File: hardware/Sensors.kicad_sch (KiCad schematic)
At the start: 21 parts, among them J10 Right Photo Cell, J11 Front Center Distance Sensor, J12 Back Center Distance Sensor, J13 Bumper Switch 1, J14 Bumper Switch 2, J15 Bumper Switch 3, J16 PIR Sensor, J17 Front Right Distance Sensor, J18 Back Right Distance Sensor, J19 Left Cliff Sensor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

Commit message: First revision of the shield PCB
I have a few more tweaks that I would like to make before I send this
off to be manufactured. I ended up going with a 4 layer board as it has
signal wires going all over the place since I was a bit contrained with
part placement by most of the Arduino signal pins being on the right
side of the board and wanting to place connectors on the side closest
to the part to which they connect.
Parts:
- removed J12: Back Center Distance Sensor, Connector_PinSocket_2.54mm:PinSocket_1x07_P2.54mm_Vertical, symbol Connector_Generic:Conn_01x07
- J13, J14, J15: footprint Connector_PinSocket_2.54mm:PinSocket_1x02_P2.54mm_Vertical -> Connector_PinSocket_2.54mm:PinSocket_1x02_P2.54mm_Horizontal
- J19, J20: footprint Connector_PinSocket_2.54mm:PinSocket_1x07_P2.54mm_Vertical -> Connector_PinSocket_2.54mm:PinSocket_1x07_P2.54mm_Horizontal
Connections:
- net BC_GPIO1 is gone; now on net BR_GPIO1: U1.7 (GPB4)
- net BC_XSHUT is gone; now on net BR_XSHUT: U1.24 (GPA4)
- net BR_GPIO1: no longer U1.8 (GPB5)
- net BR_XSHUT: no longer U1.25 (GPA5)
- net LCLIFF_GPIO1: now also U1.8 (GPB5); no longer U1.9 (GPB6)
- net LCLIFF_XSHUT: now also U1.25 (GPA5); no longer U1.26 (GPA6)
- net RCLIFF_GPIO1: now also U1.9 (GPB6); no longer U1.10 (GPB7)
- net RCLIFF_XSHUT: now also U1.26 (GPA6); no longer U1.27 (GPA7)
- no-connect marks 14 -> 15

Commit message: Cleanup PCB layout
* Made the board outline a bit smaller.
* Added the 3D .step files for all of the parts that I could find. This
  was all the parts except for the IMU from Adafruit.
* Fixed an issue where I had the back distance sensors facing in the
  wrong direction.
* Added CC BY-SA licensing info for the KiCad design files.
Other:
- title: (none) -> RugRover Shield
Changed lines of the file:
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@@
   (paper "A")
   (title_block
+    (title "RugRover Shield")
     (date "2022-03-29")
     (rev "0.1")
+    (comment 1 "CC BY-SA 4.0")
   )
   (junction (at 187.96 83.82) (diameter 0) (color 0 0 0 0)

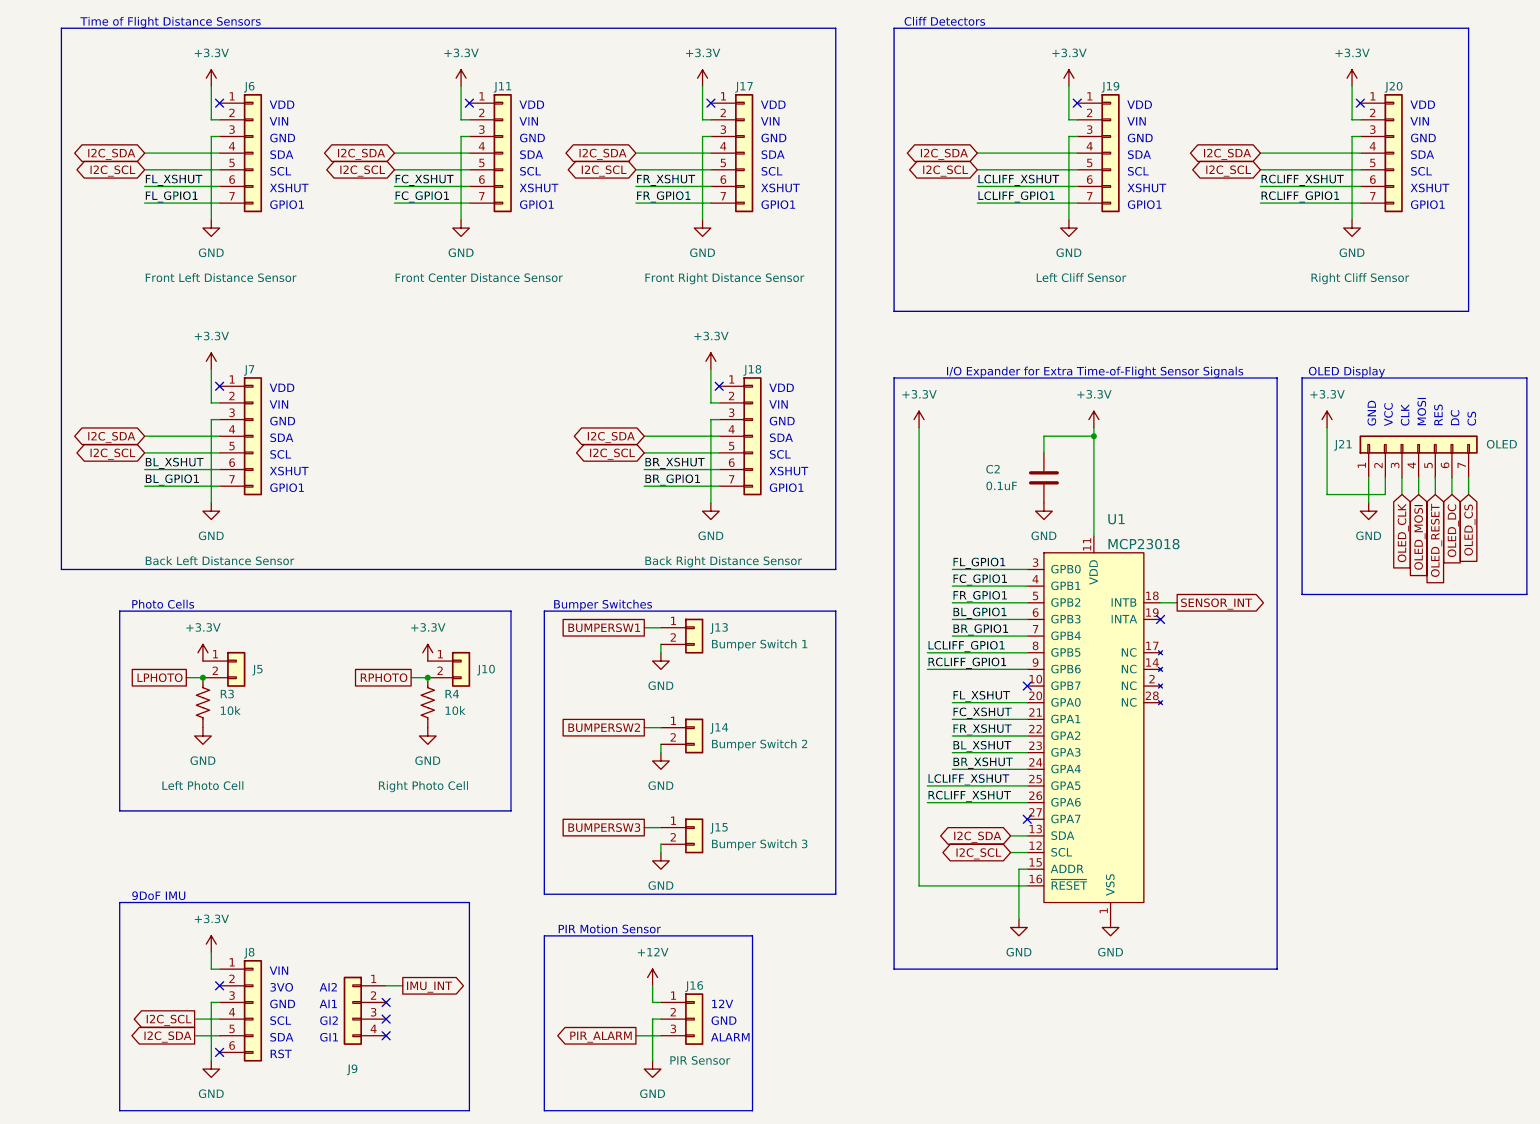
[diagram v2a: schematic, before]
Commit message: Re-align schematic to PCB
While laying out the PCB, I modified the footprints used for the
headers connecting to the nRF52-DK and changed some of the header value
names. This commit makes the same updates to the schematic sheets.
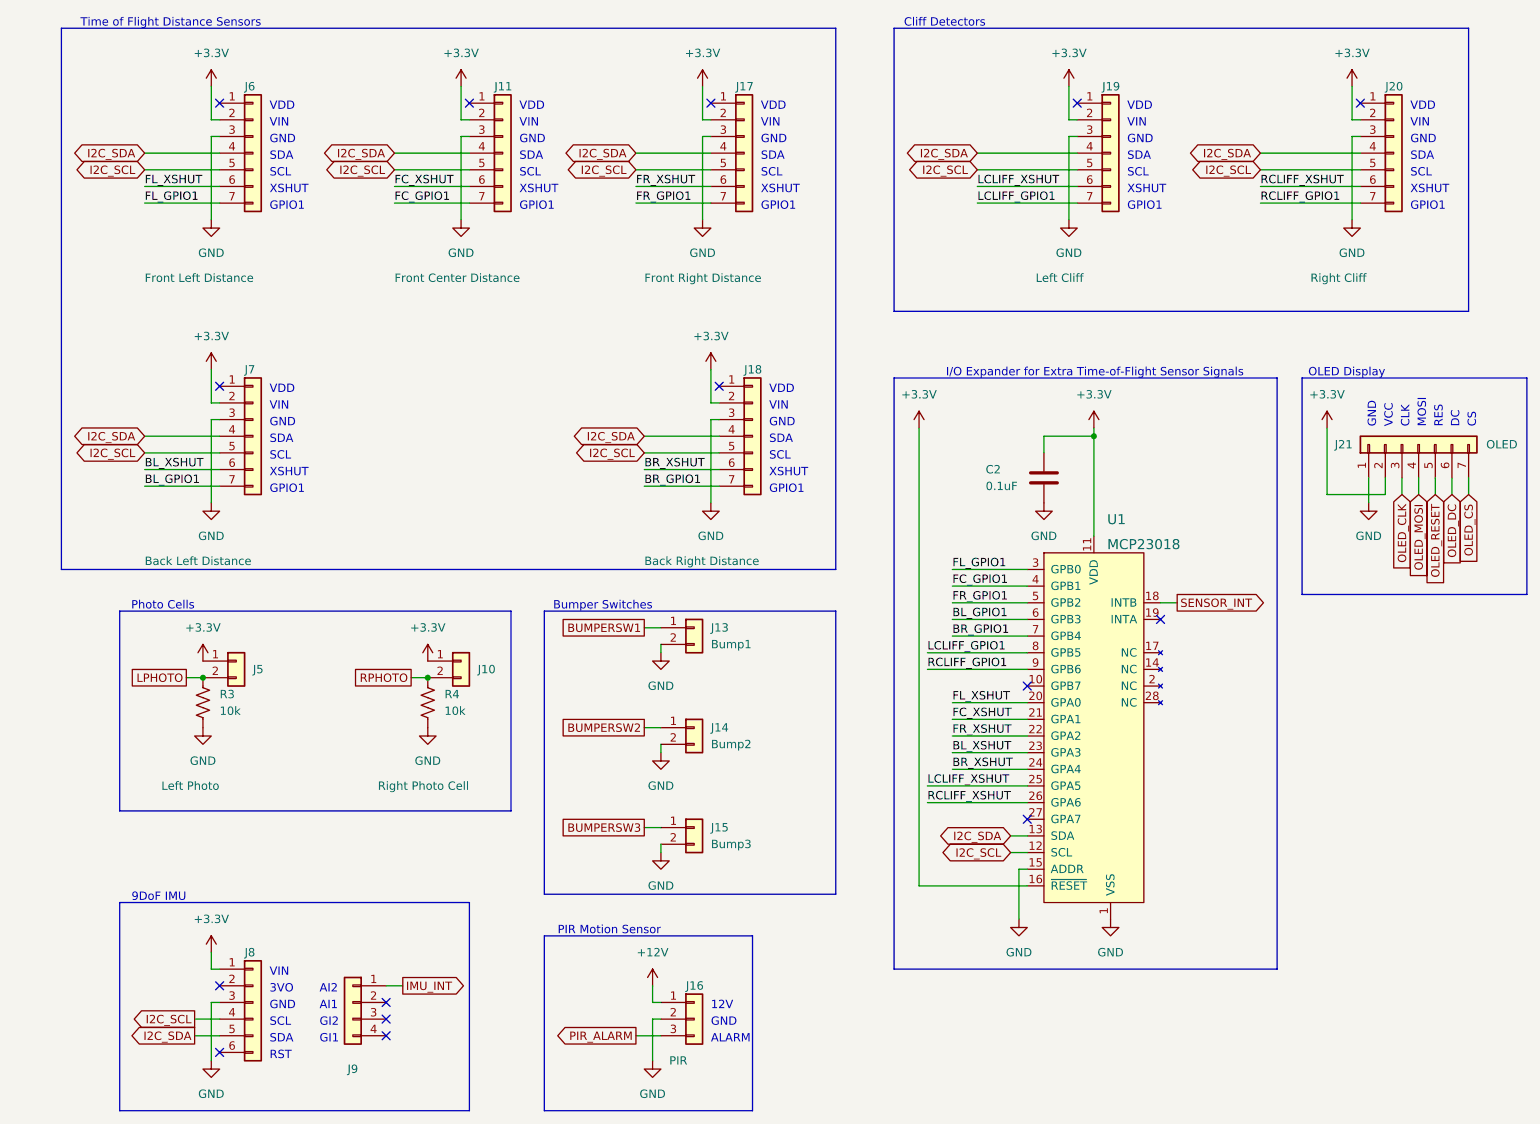
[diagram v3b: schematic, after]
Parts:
- J11: value Front Center Distance Sensor -> Front Center Distance
- J13: value Bumper Switch 1 -> Bump1
- J14: value Bumper Switch 2 -> Bump2
- J15: value Bumper Switch 3 -> Bump3
- J16: value PIR Sensor -> PIR
- J17: value Front Right Distance Sensor -> Front Right Distance
- J18: value Back Right Distance Sensor -> Back Right Distance
- J19: value Left Cliff Sensor -> Left Cliff
- J20: value Right Cliff Sensor -> Right Cliff
- J5: value Left Photo Cell -> Left Photo
- J6: value Front Left Distance Sensor -> Front Left Distance
- J7: value Back Left Distance Sensor -> Back Left Distance
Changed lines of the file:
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@@
       (effects (font (size 1.27 1.27)) (justify left))
     )
-    (property "Value" "Front Right Distance Sensor" (id 1) (at 119.38 59.69 0)
+    (property "Value" "Front Right Distance" (id 1) (at 119.38 59.69 0)
       (effects (font (size 1.27 1.27)) (justify left))
     )
@@
       (effects (font (size 1.27 1.27)) (justify left))
     )
-    (property "Value" "Bumper Switch 3" (id 1) (at 129.54 146.0499 0)
+    (property "Value" "Bump3" (id 1) (at 129.54 146.0499 0)
       (effects (font (size 1.27 1.27)) (justify left))
     )
@@
       (effects (font (size 1.27 1.27)) (justify left))
     )
-    (property "Value" "Back Left Distance Sensor" (id 1) (at 43.18 102.87 0)
+    (property "Value" "Back Left Distance" (id 1) (at 43.18 102.87 0)
       (effects (font (size 1.27 1.27)) (justify left))
     )
@@
       (effects (font (size 1.27 1.27)) (justify left))
     )
-    (property "Value" "Bumper Switch 2" (id 1) (at 129.54 130.8099 0)
+    (property "Value" "Bump2" (id 1) (at 129.54 130.8099 0)
       (effects (font (size 1.27 1.27)) (justify left))
     )
@@
       (effects (font (size 1.27 1.27)) (justify left))
     )
-    (property "Value" "Back Right Distance Sensor" (id 1) (at 119.38 102.87 0)
+    (property "Value" "Back Right Distance" (id 1) (at 119.38 102.87 0)
       (effects (font (size 1.27 1.27)) (justify left))
     )
@@
       (effects (font (size 1.27 1.27)) (justify left))
     )
-    (property "Value" "Front Left Distance Sensor" (id 1) (at 43.18 59.69 0)
+    (property "Value" "Front Left Distance" (id 1) (at 43.18 59.69 0)
       (effects (font (size 1.27 1.27)) (justify left))
     )
@@
       (effects (font (size 1.27 1.27)) (justify left))
     )
-    (property "Value" "Bumper Switch 1" (id 1) (at 129.54 115.5699 0)
+    (property "Value" "Bump1" (id 1) (at 129.54 115.5699 0)
       (effects (font (size 1.27 1.27)) (justify left))
     )
@@
       (effects (font (size 1.27 1.27)) (justify left))
     )
-    (property "Value" "Left Cliff Sensor" (id 1) (at 179.07 59.69 0)
+    (property "Value" "Left Cliff" (id 1) (at 179.07 59.69 0)
       (effects (font (size 1.27 1.27)) (justify left))
     )
@@
       (effects (font (size 1.27 1.27)) (justify left))
     )
-    (property "Value" "Front Center Distance Sensor" (id 1) (at 81.28 59.69 0)
+    (property "Value" "Front Center Distance" (id 1) (at 81.28 59.69 0)
       (effects (font (size 1.27 1.27)) (justify left))
     )
@@
       (effects (font (size 1.27 1.27)) (justify left))
     )
-    (property "Value" "Left Photo Cell" (id 1) (at 45.72 137.16 0)
+    (property "Value" "Left Photo" (id 1) (at 45.72 137.16 0)
       (effects (font (size 1.27 1.27)) (justify left))
     )
@@
       (effects (font (size 1.27 1.27)) (justify left))
     )
-    (property "Value" "Right Cliff Sensor" (id 1) (at 220.98 59.69 0)
+    (property "Value" "Right Cliff" (id 1) (at 220.98 59.69 0)
       (effects (font (size 1.27 1.27)) (justify left))
     )
@@
       (effects (font (size 1.27 1.27)) (justify left))
     )
-    (property "Value" "PIR Sensor" (id 1) (at 123.19 179.07 0)
-      (effects (font (size 1.27 1.27)) (justify left))
-    )
+    (property "Value" "PIR" (id 1) (at 123.19 179.07 0)
+      (effects (font (size 1.27 1.27)) (justify left))
+    )
